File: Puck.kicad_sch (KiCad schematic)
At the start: 15 parts, among them J1 TYPE-C-31-M-12, J2 Conn_01x05_Socket, U1 ESP32-S3-WROOM-1, U2 MCP9808T-E_MS, U4 AP2112K-3.3TRG1

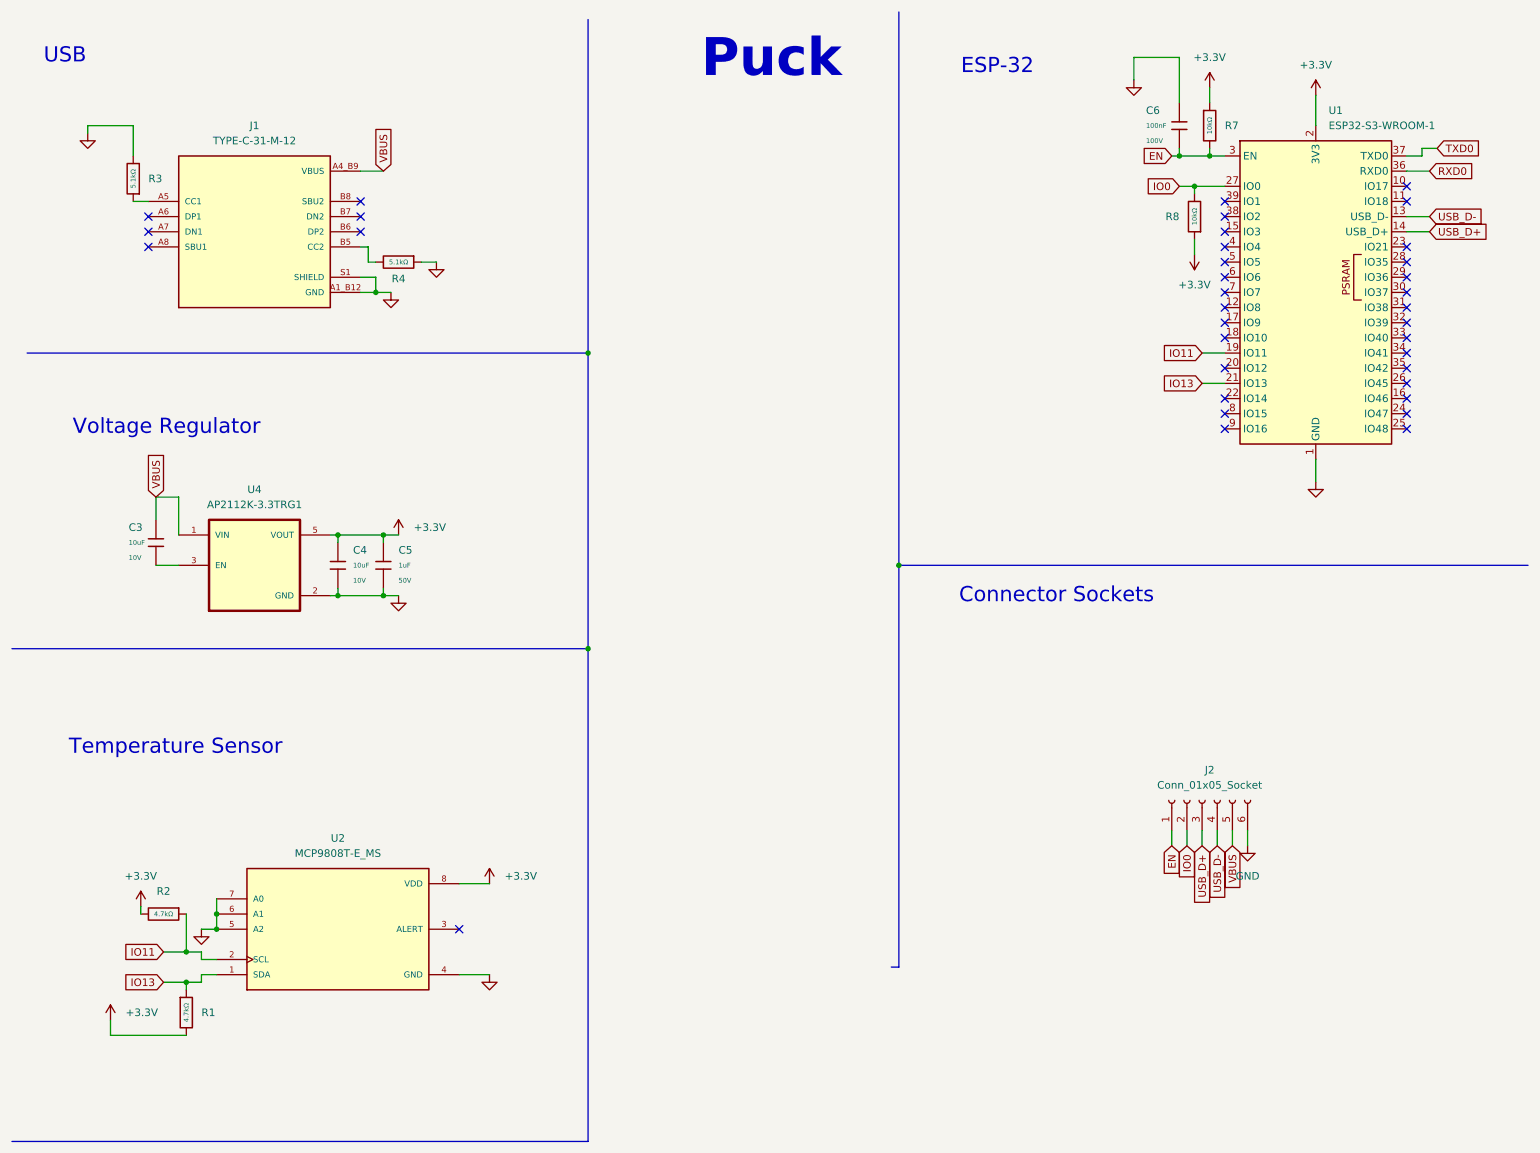
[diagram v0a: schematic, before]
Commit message: Finished schematic + redid pcb layout
Original-author: Zachariah K. Sharma <zachariah.sharma@gmail.com>
Source-commit: d32a3a69c26190fe9d53ad46781c94031068a0a4
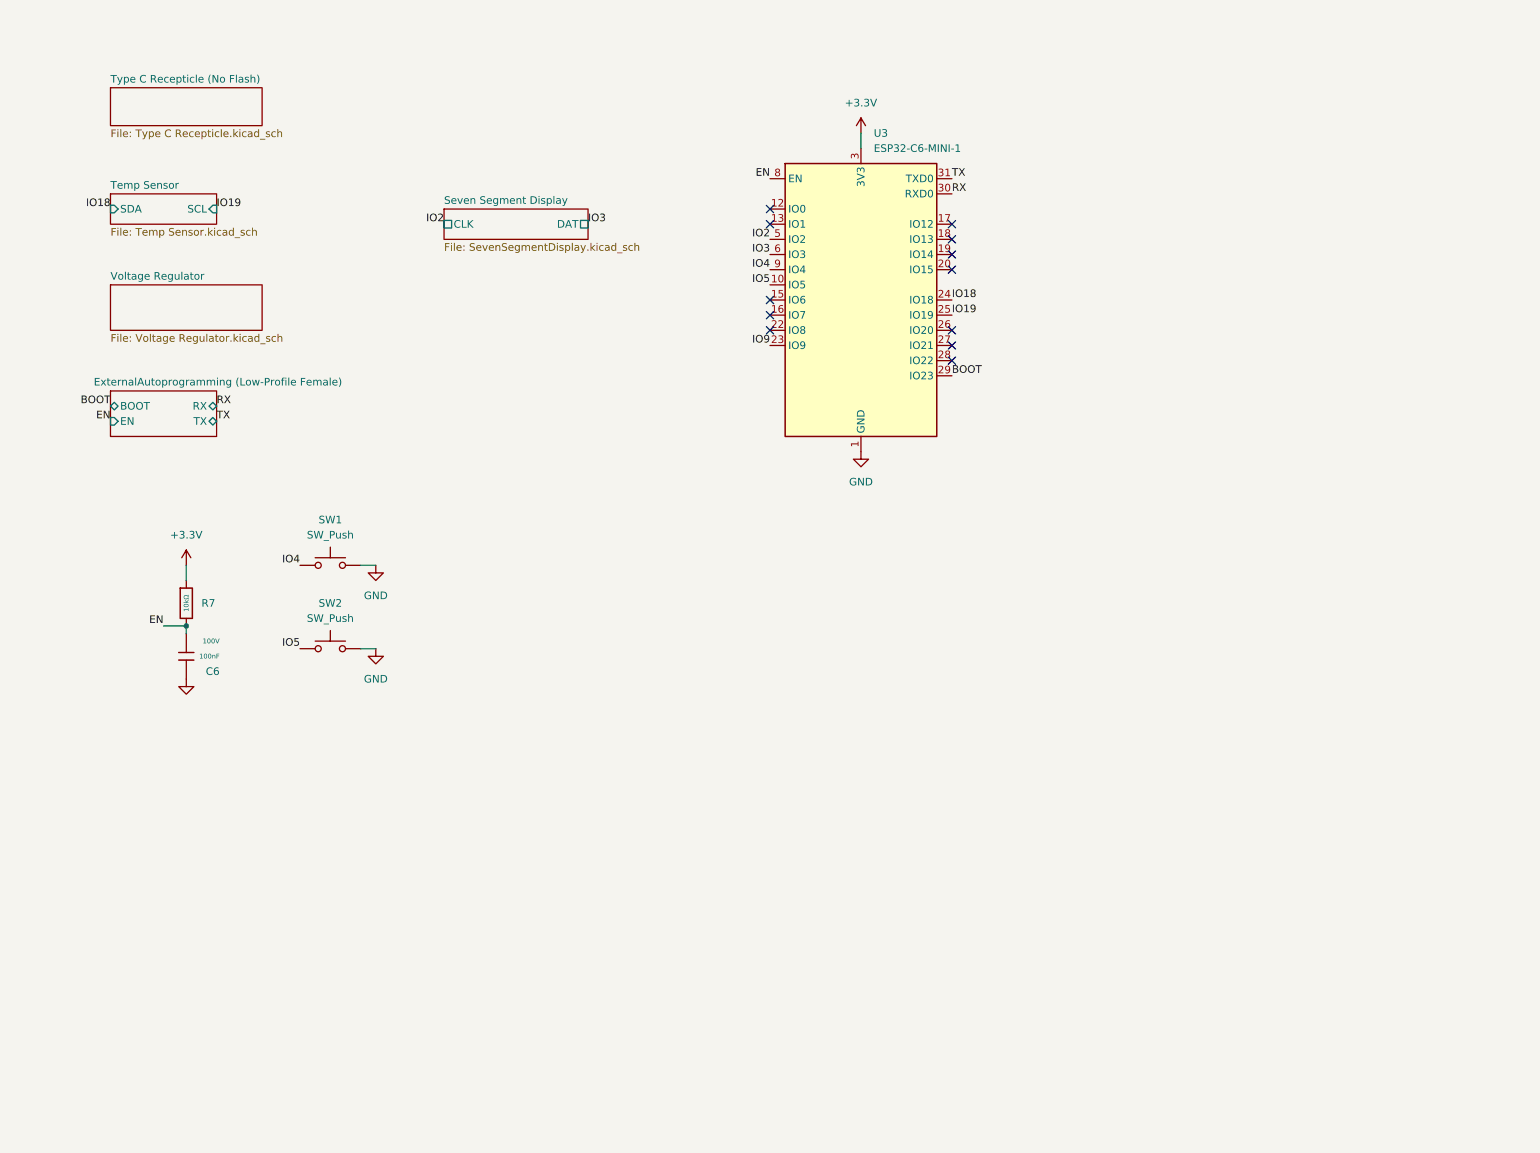
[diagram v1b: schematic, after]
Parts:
- removed C3, C4: 10uF, PCM_JLCPCB:C_0603, symbol PCM_JLCPCB-Capacitors:0603,10uF
- removed C5: 1uF, PCM_JLCPCB:C_0603, symbol PCM_JLCPCB-Capacitors:0603,1uF
- removed J1: TYPE-C-31-M-12, Footprints:HRO_TYPE-C-31-M-12, symbol TYPE-C-31-M-12:TYPE-C-31-M-12
- removed J2: Conn_01x05_Socket, Connector_JST:JST_EH_B6B-EH-A_1x06_P2.50mm_Vertical, symbol Connector:Conn_01x06_Socket
- removed R1, R2: 4.7kΩ, PCM_JLCPCB:R_0402, symbol PCM_JLCPCB-Resistors:0402,4.7kΩ
- removed R3, R4: 5.1kΩ, PCM_JLCPCB:R_0603, symbol PCM_JLCPCB-Resistors:0603,5.1kΩ
- removed R8: 10kΩ, PCM_JLCPCB:R_0603, symbol PCM_JLCPCB-Resistors:0603,10kΩ
- removed U1: ESP32-S3-WROOM-1, RF_Module:ESP32-S3-WROOM-1, symbol RF_Module:ESP32-S3-WROOM-1
- removed U2: MCP9808T-E_MS, Footprints:SOP65P490X110-8N, symbol MCP9808T-E_MS:MCP9808T-E_MS
- removed U4: AP2112K-3.3TRG1, Footprints:SOT95P285X140-5N, symbol AP2112K-3.3TRG1:AP2112K-3.3TRG1
- added SW1, SW2: SW_Push, Footprints:SW_TS-1187A-B-A-B_2term, symbol Switch:SW_Push
- added U3: ESP32-C6-MINI-1, RF_Module:ESP32-C6-MINI-1, symbol ESP32-C6-MINI-1:ESP32-C6-MINI-1
- C6: MPN (none) -> CL21B104KCFNNNE
- R7: MPN (none) -> 0603WAF1002T5E
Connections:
- net +3.3V: now also U3.3 (3V3)
- net EN: now also U3.8 (EN)
- net GND: now also SW1.2, SW2.2, U3.1 (GND), U3.11 (GND), U3.14 (GND), U3.2 (GND), U3.36 (GND), U3.37 (GND), U3.38 (GND), U3.39 (GND), U3.40 (GND), U3.41 (GND), U3.42 (GND), U3.43 (GND), U3.44 (GND), U3.45 (GND), U3.46 (GND), U3.47 (GND), U3.48 (GND), U3.49 (GND), U3.50 (GND), U3.51 (GND), U3.52 (GND), U3.53 (GND)
- new net BOOT: U3.29 (IO23)
- new net IO18: U3.24 (IO18)
- new net IO19: U3.25 (IO19)
- new net IO2: U3.5 (IO2)
- new net IO3: U3.6 (IO3)
- new net IO4: SW1.1, U3.9 (IO4)
- new net IO5: SW2.1, U3.10 (IO5)
- new net IO9: U3.23 (IO9)
- new net RX: U3.30 (RXD0)
- new net TX: U3.31 (TXD0)
- no-connect marks 36 -> 12
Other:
- added sheet ExternalAutoprogramming (Low-Profile Female) (ExternalAutoprogramming.kicad_sch)
- added sheet Seven Segment Display (SevenSegmentDisplay.kicad_sch)
- added sheet Temp Sensor (Temp Sensor.kicad_sch)
- added sheet Type C Recepticle (No Flash) (Type C Recepticle.kicad_sch)
- added sheet Voltage Regulator (Voltage Regulator.kicad_sch)
- note removed: "Connector Sockets"
- note removed: "ESP-32"
- note removed: "Puck"
- note removed: "Temperature Sensor"
- note removed: "USB"
- note removed: "Voltage Regulator"

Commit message: feat: Add metadata for schematic sheets
Original-author: Ishan Karmakar <ishan.karmakar24@gmail.com>
Source-commit: c82f4670f2f6b6f19a8645b0d3909227ee38d77d
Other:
- title: Vynte Puck -> Puck
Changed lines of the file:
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@@
 	(paper "A5")
 	(title_block
-		(title "Vynte Puck")
-		(date "2026-02-19")
+		(title "Puck")
+		(date "2026-08-21")
+		(rev "${PROJECT_REV}")
 		(company "Vynte")
-		(comment 1 "Designed by: Zachariah Sharma")
 	)
 	(junction

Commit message: fix: Fix most design issues
Original-author: Ishan Karmakar <ishan.karmakar24@gmail.com>
Source-commit: a70ad4e322e6afcc76e9c4ecaab6da1a8e108794
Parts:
- removed U3: ESP32-C6-MINI-1, RF_Module:ESP32-C6-MINI-1, symbol ESP32-C6-MINI-1:ESP32-C6-MINI-1
- added U2: ESP32-C6-MINI-1/U, PCM_Espressif:ESP32-C6-MINI-1, symbol PCM_Espressif:ESP32-C6-MINI-1/U
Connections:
- net +3.3V: now also U2.3 (3V3)
- net BOOT: now also U2.29 (GPIO23)
- net EN: now also U2.8 (EN/CHIP_PU)
- net GND: now also U2.1 (GND), U2.11 (GND), U2.14 (GND), U2.2 (GND), U2.36 (GND), U2.37 (GND), U2.38 (GND), U2.39 (GND), U2.40 (GND), U2.41 (GND), U2.42 (GND), U2.43 (GND), U2.44 (GND), U2.45 (GND), U2.46 (GND), U2.47 (GND), U2.48 (GND), U2.49 (GND), U2.50 (GND), U2.51 (GND), U2.52 (GND), U2.53 (GND)
- net IO18: now also U2.24 (GPIO18)
- net IO19: now also U2.25 (GPIO19)
- net IO2: now also U2.5 (GPIO2/ADC1_CH2)
- net IO3: now also U2.6 (GPIO3/ADC1_CH3)
- net IO4: now also U2.9 (MTMS/GPIO4/ADC1_CH4)
- net IO5: now also U2.10 (MTDI/GPIO5/ADC1_CH5)
- net IO9: now also U2.23 (GPIO9)
- net RX: now also U2.30 (U0RXD/GPIO17)
- net TX: now also U2.31 (U0TXD/GPIO16)

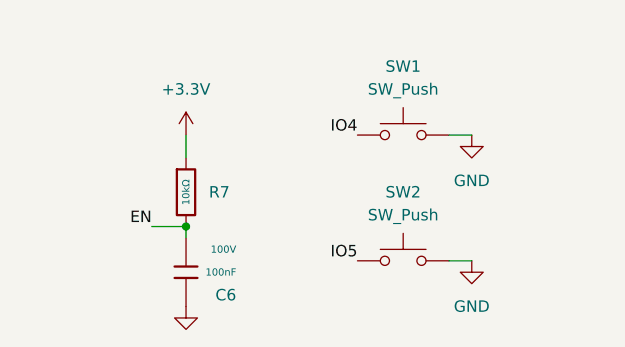
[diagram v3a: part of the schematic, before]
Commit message: feat: Use standard KiCad capacitor symbols and footprints
Original-author: Ishan Karmakar <ishan.karmakar24@gmail.com>
Source-commit: 6d92738db7c1a3a0126f93a2d140869e5f4c1fb9
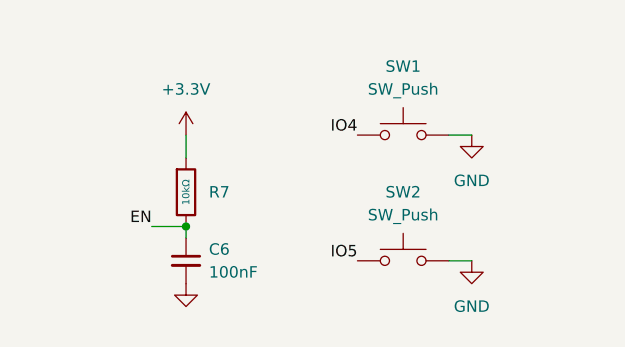
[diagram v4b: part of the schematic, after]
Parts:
- removed C6: 100nF, PCM_JLCPCB:C_0805, symbol PCM_JLCPCB-Capacitors:0805,100nF
- added C6: 100nF, Capacitor_SMD:C_0603_1608Metric, symbol Device:C_Small
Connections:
- net EN: now also C6.1
- net GND: now also C6.2
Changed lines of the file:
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@@
-	)
-	(symbol
-		(lib_id "PCM_JLCPCB-Capacitors:0805,100nF")
-		(at 41.91 119.38 0)
-		(unit 1)
-		(body_style 1)
-		(exclude_from_sim no)
-		(in_bom yes)
-		(on_board yes)
-		(in_pos_files yes)
-		(dnp no)
-		(property "Reference" "C6"
-			(at 47.498 121.9201 0)
-			(show_name no)
-			(do_not_autoplace no)
-			(effects
-				(font
-					(size 1.27 1.27)
-				)
-				(justify right)
-			)
-		)
-		(property "Value" "100nF"
-			(at 47.498 119.38 0)
-			(show_name no)
-			(do_not_autoplace no)
-			(effects
-				(font
-					(size 0.8 0.8)
-				)
-				(justify right)
-			)
-		)
-		(property "Footprint" "PCM_JLCPCB:C_0805"
-			(at 40.132 119.38 90)
-			(hide yes)
-			(show_name no)
-			(do_not_autoplace no)
-			(effects
-				(font
-					(size 1.27 1.27)
-				)
-			)
-		)
-		(property "Datasheet" "https://www.lcsc.com/datasheet/lcsc_datasheet_2304140030_Samsung-Electro-Mechanics-CL21B104KCFNNNE_C28233.pdf"
-			(at 41.91 119.38 0)
-			(hide yes)
-			(show_name no)
-			(do_not_autoplace no)
-			(effects
-				(font
-					(size 1.27 1.27)
-				)
-			)
-		)
-		(property "Description" "100V 100nF X7R ±10% 0805 Multilayer Ceramic Capacitors MLCC - SMD/SMT ROHS"
-			(at 41.91 119.38 0)
-			(hide yes)
-			(show_name no)
-			(do_not_autoplace no)
-			(effects
-				(font
-					(size 1.27 1.27)
-				)
-			)
-		)
-		(property "MPN" "CL21B104KCFNNNE"
-			(at 47.498 119.38 0)
-			(hide yes)
-			(show_name no)
-			(do_not_autoplace no)
-			(effects
-				(font
-					(size 1.27 1.27)
-				)
-			)
-		)
-		(property "LCSC" "C28233"
-			(at 41.91 119.38 0)
-			(hide yes)
-			(show_name no)
-			(do_not_autoplace no)
-			(effects
-				(font
-					(size 1.27 1.27)
-				)
-			)
-		)
-		(property "Stock" "1168020"
-			(at 41.91 119.38 0)
-			(hide yes)
-			(show_name no)
-			(do_not_autoplace no)
-			(effects
-				(font
-					(size 1.27 1.27)
-				)
-			)
-		)
-		(property "Price" "0.009USD"
-			(at 41.91 119.38 0)
-			(hide yes)
-			(show_name no)
-			(do_not_autoplace no)
-			(effects
-				(font
-					(size 1.27 1.27)
-				)
-			)
-		)
-		(property "Process" "SMT"
-			(at 41.91 119.38 0)
-			(hide yes)
-			(show_name no)
-			(do_not_autoplace no)
-			(effects
-				(font
-					(size 1.27 1.27)
-				)
-			)
-		)
-		(property "Minimum Qty" "20"
-			(at 41.91 119.38 0)
-			(hide yes)
-			(show_name no)
-			(do_not_autoplace no)
-			(effects
-				(font
-					(size 1.27 1.27)
-				)
-			)
-		)
-		(property "Attrition Qty" "10"
-			(at 41.91 119.38 0)
-			(hide yes)
-			(show_name no)
-			(do_not_autoplace no)
-			(effects
-				(font
-					(size 1.27 1.27)
-				)
-			)
-		)
-		(property "Class" "Basic Component"
-			(at 41.91 119.38 0)
-			(hide yes)
-			(show_name no)
-			(do_not_autoplace no)
-			(effects
-				(font
-					(size 1.27 1.27)
-				)
-			)
-		)
-		(property "Category" "Capacitors,Multilayer Ceramic Capacitors MLCC - SMD/SMT"
-			(at 41.91 119.38 0)
-			(hide yes)
-			(show_name no)
-			(do_not_autoplace no)
-			(effects
-				(font
-					(size 1.27 1.27)
-				)
-			)
-		)
-		(property "Manufacturer" "Samsung Electro-Mechanics"
-			(at 41.91 119.38 0)
-			(hide yes)
-			(show_name no)
-			(do_not_autoplace no)
-			(effects
-				(font
-					(size 1.27 1.27)
-				)
-			)
-		)
-		(property "Part" "CL21B104KCFNNNE"
-			(at 41.91 119.38 0)
-			(hide yes)
-			(show_name no)
-			(do_not_autoplace no)
-			(effects
-				(font
-					(size 1.27 1.27)
-				)
-			)
-		)
-		(property "Voltage Rated" "100V"
-			(at 47.498 116.84 0)
-			(show_name no)
-			(do_not_autoplace no)
-			(effects
-				(font
-					(size 0.8 0.8)
-				)
-				(justify right)
-			)
-		)
-		(property "Tolerance" "±10%"
-			(at 41.91 119.38 0)
-			(hide yes)
-			(show_name no)
-			(do_not_autoplace no)
-			(effects
-				(font
-					(size 1.27 1.27)
-				)
-			)
-		)
-		(property "Capacitance" "100nF"
-			(at 41.91 119.38 0)
-			(hide yes)
-			(show_name no)
-			(do_not_autoplace no)
-			(effects
-				(font
-					(size 1.27 1.27)
-				)
-			)
-		)
-		(property "Temperature Coefficient" "X7R"
-			(at 41.91 119.38 0)
-			(hide yes)
-			(show_name no)
-			(do_not_autoplace no)
-			(effects
-				(font
-					(size 1.27 1.27)
-				)
-			)
-		)
-		(pin "1"
-		)
-		(pin "2"
-		)
-		(instances
-			(project "Puck"
-				(path "/25eaca85-d617-4fff-8dd9-d1f31cfc8927"
-					(reference "C6")
-					(unit 1)
-				)
-			)
-		)
 	)
 	(symbol
@@
 	)
 	(symbol
+		(lib_id "Device:C_Small")
+		(at 41.91 118.11 0)
+		(unit 1)
+		(body_style 1)
+		(exclude_from_sim no)
+		(in_bom yes)
+		(on_board yes)
+		(in_pos_files yes)
+		(dnp no)
+		(fields_autoplaced yes)
+		(property "Reference" "C6"
+			(at 44.45 116.8462 0)
+			(show_name no)
+			(do_not_autoplace no)
+			(effects
+				(font
+					(size 1.27 1.27)
+				)
+				(justify left)
+			)
+		)
+		(property "Value" "100nF"
+			(at 44.45 119.3862 0)
+			(show_name no)
+			(do_not_autoplace no)
+			(effects
+				(font
+					(size 1.27 1.27)
+				)
+				(justify left)
+			)
+		)
+		(property "Footprint" "Capacitor_SMD:C_0603_1608Metric"
+			(at 41.91 118.11 0)
+			(hide yes)
+			(show_name no)
+			(do_not_autoplace no)
+			(effects
+				(font
+					(size 1.27 1.27)
+				)
+			)
+		)
+		(property "Datasheet" ""
+			(at 41.91 118.11 0)
+			(hide yes)
+			(show_name no)
+			(do_not_autoplace no)
+			(effects
+				(font
+					(size 1.27 1.27)
+				)
+			)
+		)
+		(property "Description" "Unpolarized capacitor, small symbol"
+			(at 41.91 118.11 0)
+			(hide yes)
+			(show_name no)
+			(do_not_autoplace no)
+			(effects
+				(font
+					(size 1.27 1.27)
+				)
+			)
+		)
+		(pin "1"
+		)
+		(pin "2"
+		)
+		(instances
+			(project "Puck"
+				(path "/25eaca85-d617-4fff-8dd9-d1f31cfc8927"
+					(reference "C6")
+					(unit 1)
+				)
+			)
+		)
+	)
+	(symbol
 		(lib_id "Switch:SW_Push")
 		(at 66.04 104.14 0)
@@
 	(symbol
 		(lib_id "power:GND")
-		(at 41.91 123.19 0)
+		(at 41.91 120.65 0)
 		(unit 1)
 		(body_style 1)
@@
 		(fields_autoplaced yes)
 		(property "Reference" "#PWR015"
-			(at 41.91 129.54 0)
+			(at 41.91 127 0)
 			(hide yes)
 			(show_name no)
@@
 		)
 		(property "Value" "GND"
-			(at 44.45 124.4599 0)
+			(at 44.45 121.9199 0)
 			(hide yes)
 			(show_name no)
@@
 		)
 		(property "Footprint" ""
-			(at 41.91 123.19 0)
+			(at 41.91 120.65 0)
 			(hide yes)
 			(show_name no)
@@
 		)
 		(property "Datasheet" ""
-			(at 41.91 123.19 0)
+			(at 41.91 120.65 0)
 			(hide yes)
 			(show_name no)
@@
 		)
 		(property "Description" "Power symbol creates a global label with name \"GND\" , ground"
-			(at 41.91 123.19 0)
-			(hide yes)
-			(show_name no)
+			(at 41.91 120.65 0)
+			(hide yes)
+			(show_name no)
